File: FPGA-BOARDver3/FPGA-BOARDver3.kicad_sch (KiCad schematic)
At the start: 0 parts

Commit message: power regulation schematic added
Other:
- added sheet POWER_REGULATION (power_regulation.kicad_sch)
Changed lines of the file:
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@@
+	)
+	(sheet
+		(at 148.59 58.42)
+		(size 22.86 29.21)
+		(fields_autoplaced yes)
+		(stroke
+			(width 0.1524)
+			(type solid)
+		)
+		(fill
+			(color 0 0 0 0.0000)
+		)
+		(property "Sheetname" "POWER_REGULATION"
+			(at 148.59 57.7084 0)
+			(effects
+				(font
+					(size 1.27 1.27)
+				)
+				(justify left bottom)
+			)
+		)
+		(property "Sheetfile" "power_regulation.kicad_sch"
+			(at 148.59 88.2146 0)
+			(effects
+				(font
+					(size 1.27 1.27)
+				)
+				(justify left top)
+			)
+		)
+		(instances
+			(project "FPGA-BOARDver3"
+				(path "/4a327bdf-04e5-4836-9c0a-5fb801c23f64"
+					(page "16")
+				)
+			)
+		)
 	)
 	(sheet

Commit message: DDR3 Schematic sheet added
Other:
- added sheet DDR3 (DDR3.kicad_sch)
- added sheet POWER_REGULATION2 (POWER_REGULATION2.kicad_sch)
- sheet POWER_REGULATION: file power_regulation.kicad_sch -> POWER_REGULATION.kicad_sch
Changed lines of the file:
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@@
 			)
 		)
-		(property "Sheetfile" "power_regulation.kicad_sch"
+		(property "Sheetfile" "POWER_REGULATION.kicad_sch"
 			(at 148.59 88.2146 0)
 			(effects
@@
 	)
 	(sheet
+		(at 149.86 97.79)
+		(size 24.13 30.48)
+		(fields_autoplaced yes)
+		(stroke
+			(width 0.1524)
+			(type solid)
+		)
+		(fill
+			(color 0 0 0 0.0000)
+		)
+		(property "Sheetname" "POWER_REGULATION2"
+			(at 149.86 97.0784 0)
+			(effects
+				(font
+					(size 1.27 1.27)
+				)
+				(justify left bottom)
+			)
+		)
+		(property "Sheetfile" "POWER_REGULATION2.kicad_sch"
+			(at 149.86 128.8546 0)
+			(effects
+				(font
+					(size 1.27 1.27)
+				)
+				(justify left top)
+			)
+		)
+		(instances
+			(project "FPGA-BOARDver3"
+				(path "/4a327bdf-04e5-4836-9c0a-5fb801c23f64"
+					(page "17")
+				)
+			)
+		)
+	)
+	(sheet
 		(at 86.36 57.15)
 		(size 20.32 26.67)
@@
 				)
 			)
+		)
+	)
+	(sheet
+		(at 121.92 144.78)
+		(size 26.67 30.48)
+		(fields_autoplaced yes)
+		(stroke
+			(width 0.1524)
+			(type solid)
+		)
+		(fill
+			(color 0 0 0 0.0000)
+		)
+		(property "Sheetname" "DDR3"
+			(at 121.92 144.0684 0)
+			(effects
+				(font
+					(size 1.27 1.27)
+				)
+				(justify left bottom)
+			)
+		)
+		(property "Sheetfile" "DDR3.kicad_sch"
+			(at 121.92 175.8446 0)
+			(effects
+				(font
+					(size 1.27 1.27)
+				)
+				(justify left top)
+			)
+		)
+		(instances
+			(project "FPGA-BOARDver3"
+				(path "/4a327bdf-04e5-4836-9c0a-5fb801c23f64"
+					(page "18")
+				)
+			)

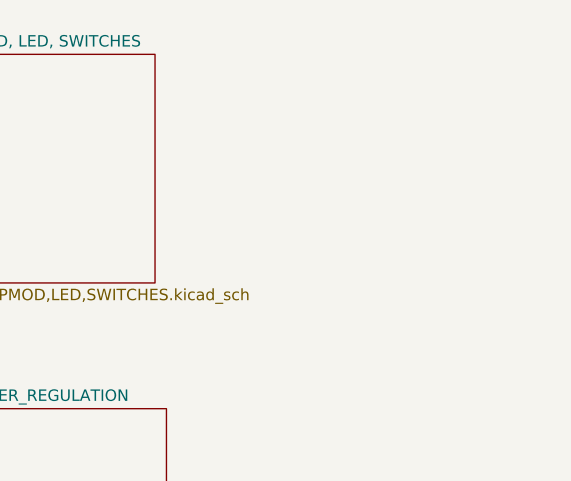
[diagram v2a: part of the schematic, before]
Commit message: Added FPGA-POWER Schematic
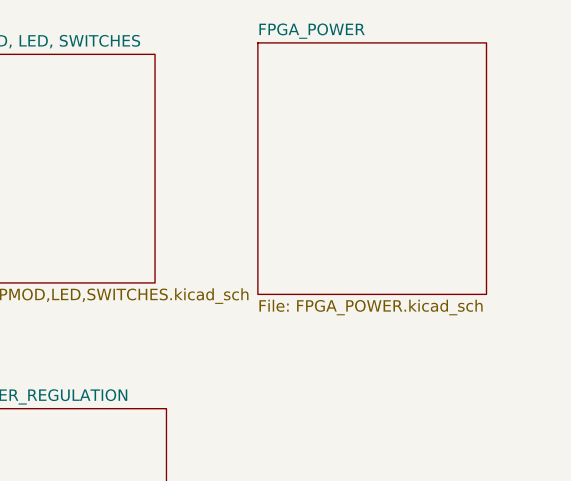
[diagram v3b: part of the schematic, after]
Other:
- added sheet FPGA_POWER (FPGA_POWER.kicad_sch)
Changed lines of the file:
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@@
+	)
+	(sheet
+		(at 181.61 17.78)
+		(size 25.4 27.94)
+		(fields_autoplaced yes)
+		(stroke
+			(width 0.1524)
+			(type solid)
+		)
+		(fill
+			(color 0 0 0 0.0000)
+		)
+		(property "Sheetname" "FPGA_POWER"
+			(at 181.61 17.0684 0)
+			(effects
+				(font
+					(size 1.27 1.27)
+				)
+				(justify left bottom)
+			)
+		)
+		(property "Sheetfile" "FPGA_POWER.kicad_sch"
+			(at 181.61 46.3046 0)
+			(effects
+				(font
+					(size 1.27 1.27)
+				)
+				(justify left top)
+			)
+		)
+		(instances
+			(project "FPGA-BOARDver3"
+				(path "/4a327bdf-04e5-4836-9c0a-5fb801c23f64"
+					(page "19")
+				)
+			)
+		)
 	)
 	(sheet

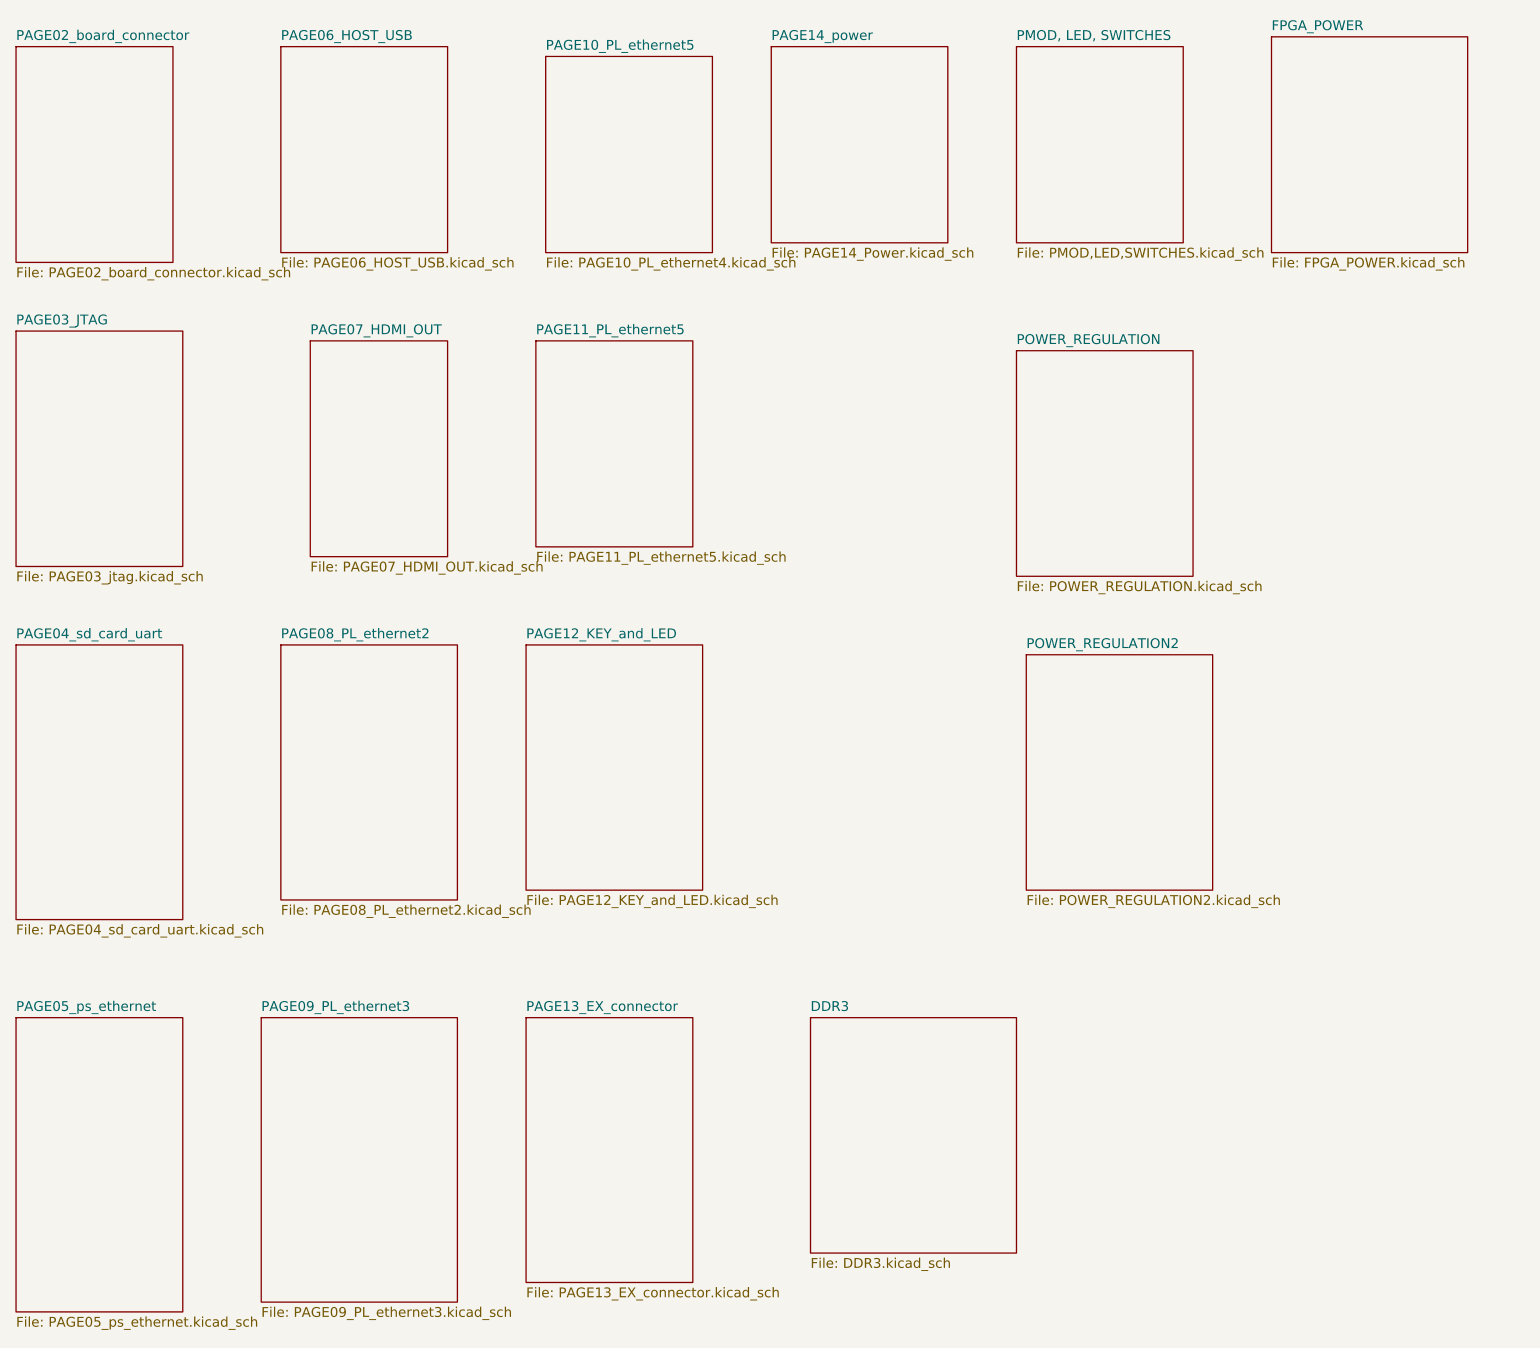
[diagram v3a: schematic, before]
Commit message: Power Regulation sheet 2 added
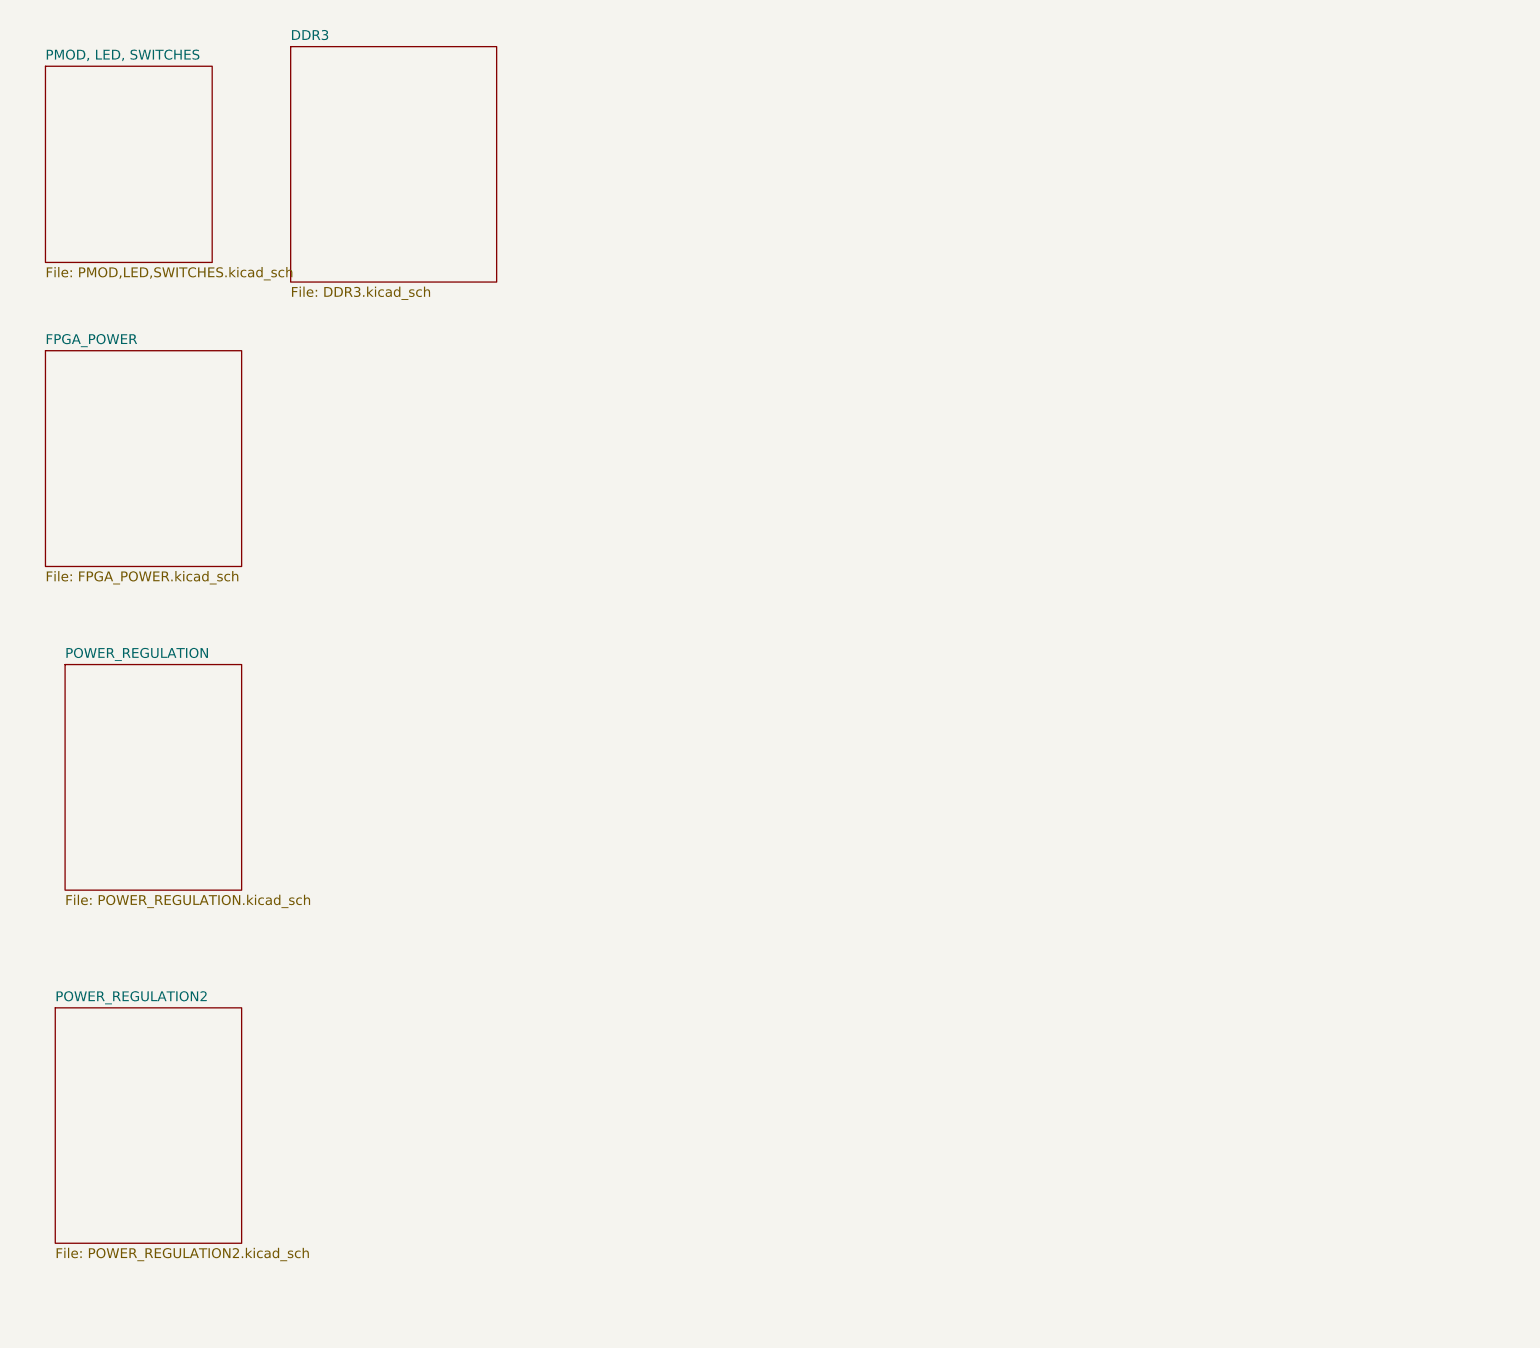
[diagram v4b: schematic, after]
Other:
- removed sheet PAGE02_board_connector
- removed sheet PAGE03_JTAG
- removed sheet PAGE04_sd_card_uart
- removed sheet PAGE05_ps_ethernet
- removed sheet PAGE06_HOST_USB
- removed sheet PAGE07_HDMI_OUT
- removed sheet PAGE08_PL_ethernet2
- removed sheet PAGE09_PL_ethernet3
- removed sheet PAGE10_PL_ethernet5
- removed sheet PAGE11_PL_ethernet5
- removed sheet PAGE12_KEY_and_LED
- removed sheet PAGE13_EX_connector
- removed sheet PAGE14_power

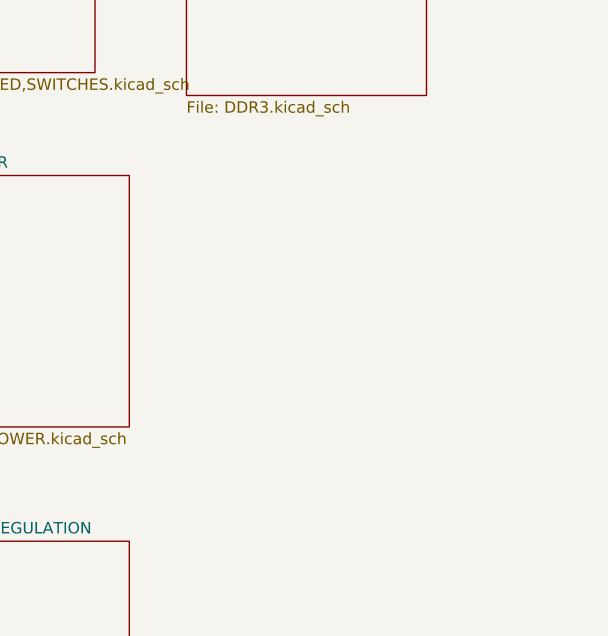
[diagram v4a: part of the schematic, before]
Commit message: added fpga banks and final fpga symbol
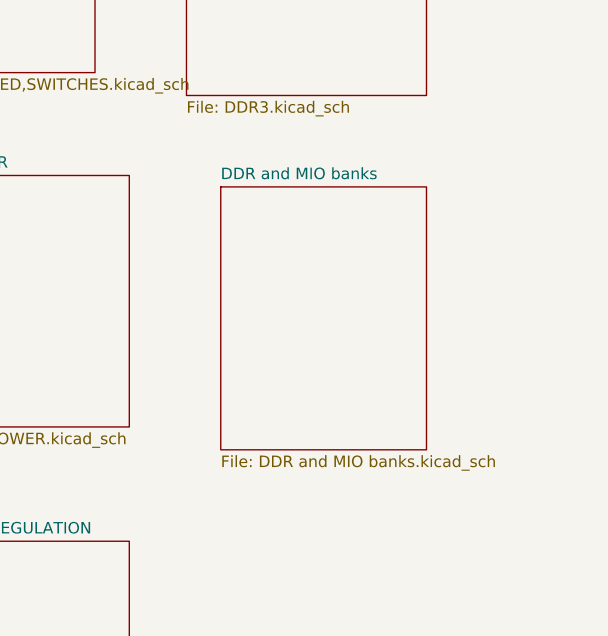
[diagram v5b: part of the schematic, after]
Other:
- added sheet DDR and MIO banks (DDR and MIO banks.kicad_sch)
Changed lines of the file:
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@@
+	)
+	(sheet
+		(at 58.42 59.69)
+		(size 22.86 29.21)
+		(fields_autoplaced yes)
+		(stroke
+			(width 0.1524)
+			(type solid)
+		)
+		(fill
+			(color 0 0 0 0.0000)
+		)
+		(property "Sheetname" "DDR and MIO banks"
+			(at 58.42 58.9784 0)
+			(effects
+				(font
+					(size 1.27 1.27)
+				)
+				(justify left bottom)
+			)
+		)
+		(property "Sheetfile" "DDR and MIO banks.kicad_sch"
+			(at 58.42 89.4846 0)
+			(effects
+				(font
+					(size 1.27 1.27)
+				)
+				(justify left top)
+			)
+		)
+		(instances
+			(project "FPGA-BOARDver3"
+				(path "/4a327bdf-04e5-4836-9c0a-5fb801c23f64"
+					(page "7")
+				)
+			)
+		)
 	)
 	(sheet

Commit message: hdmi added
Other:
- added sheet hdmi (hdmi.kicad_sch)
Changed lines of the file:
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@@
+	)
+	(sheet
+		(at 87.63 129.54)
+		(size 29.21 39.37)
+		(fields_autoplaced yes)
+		(stroke
+			(width 0.1524)
+			(type solid)
+		)
+		(fill
+			(color 0 0 0 0.0000)
+		)
+		(property "Sheetname" "hdmi"
+			(at 87.63 128.8284 0)
+			(effects
+				(font
+					(size 1.27 1.27)
+				)
+				(justify left bottom)
+			)
+		)
+		(property "Sheetfile" "hdmi.kicad_sch"
+			(at 87.63 169.4946 0)
+			(effects
+				(font
+					(size 1.27 1.27)
+				)
+				(justify left top)
+			)
+		)
+		(instances
+			(project "FPGA-BOARDver3"
+				(path "/4a327bdf-04e5-4836-9c0a-5fb801c23f64"
+					(page "8")
+				)
+			)
+		)
 	)
 	(sheet
